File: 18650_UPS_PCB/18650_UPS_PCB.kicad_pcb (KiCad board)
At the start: 4 copper layers, 90 x 27.5 mm, 40 parts, among them J1 USB_B_Micro, J2 Conn_01x02, J3 Conn_01x02, SW1 SW_DIP_x02, U1 STLINK-V3MINI, U10 LR9102G-xx, U11 MP2667, U2 INA260, U3 EA_DOGS104N-A, U5 STM32L151RCTx

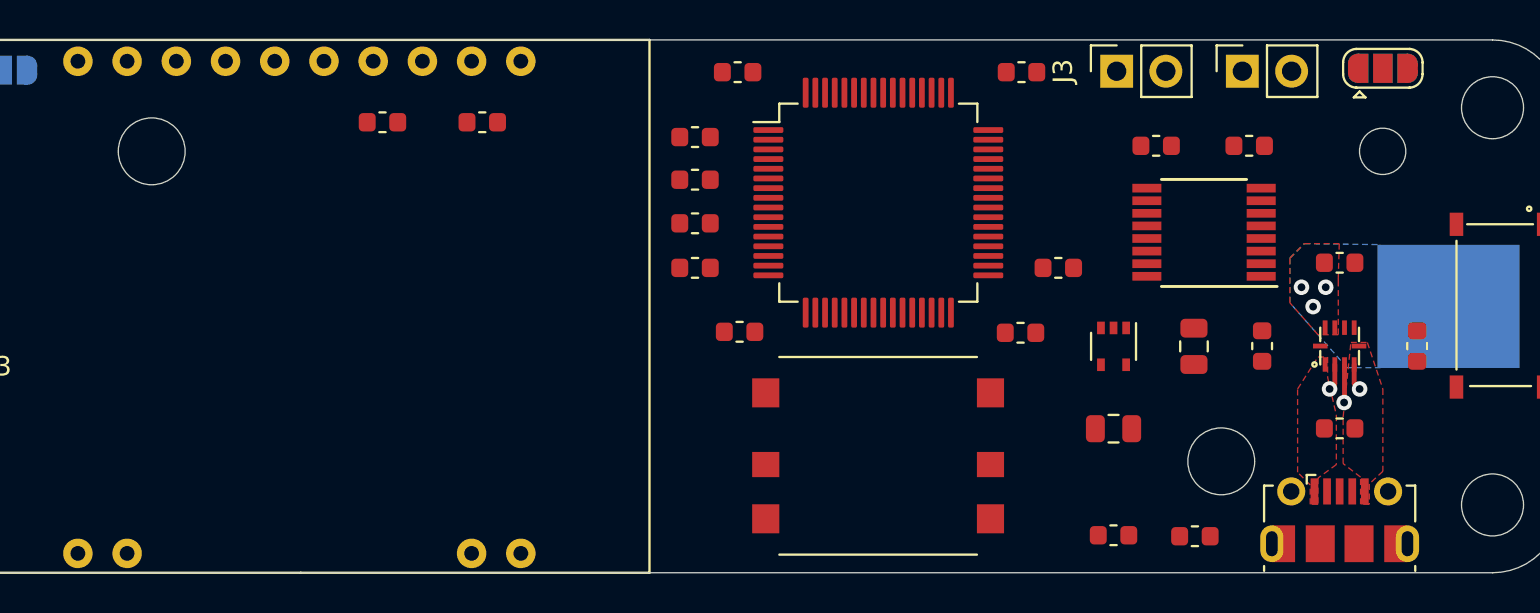
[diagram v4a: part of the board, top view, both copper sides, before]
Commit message: changed to ina 237/239
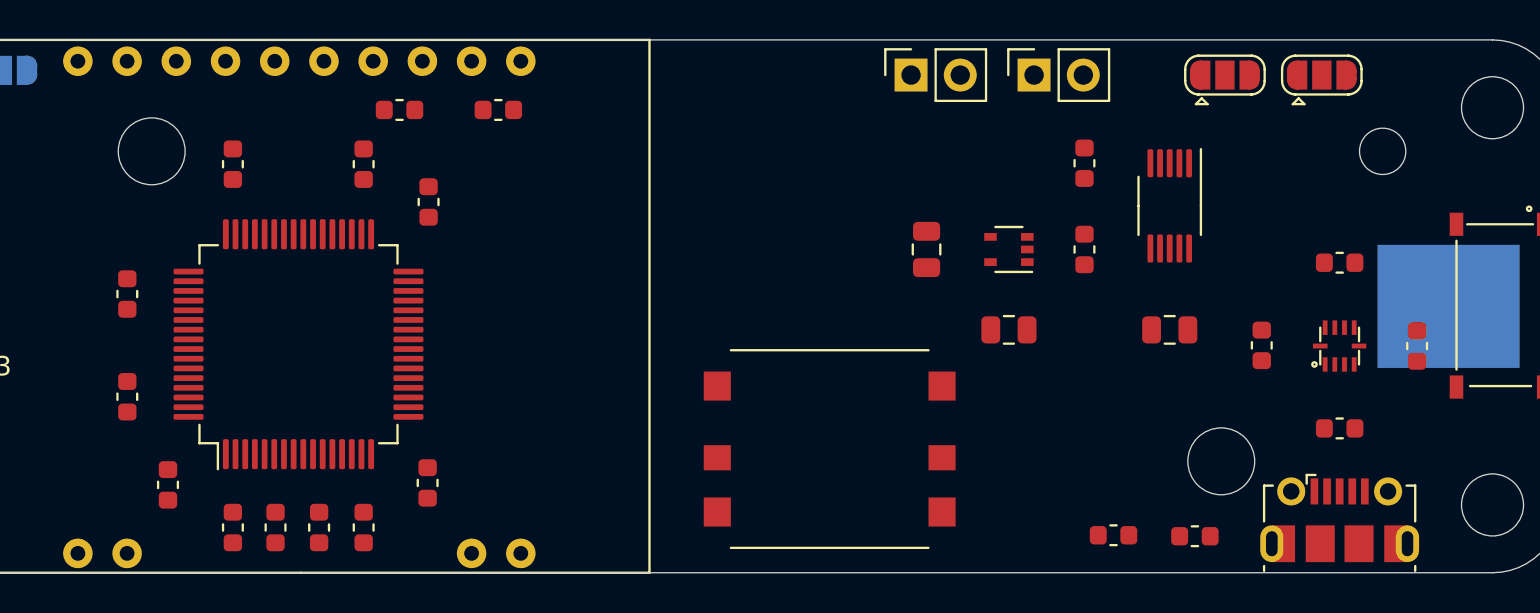
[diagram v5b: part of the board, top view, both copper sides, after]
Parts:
- added R3: 10 kOhm, Resistor_SMD:R_0603_1608Metric, F.Cu at (186.2, 80.5)
- added R4: 10 kOhm, Resistor_SMD:R_0603_1608Metric, F.Cu at (136.8, 87.3)
- added R5: 10 kOhm, Resistor_SMD:R_0603_1608Metric, F.Cu at (136.8, 92.6)
- JP2: moved to F.Cu
- R1: value 10 kOhm -> 0.01 Ohm; footprint Resistor_SMD:R_0603_1608Metric -> Resistor_SMD:R_0805_2012Metric
- U2: value INA260 -> INA237; footprint Package_SO:TSSOP-16_4.4x5mm_P0.65mm -> Package_SO:VSSOP-10_3x3mm_P0.5mm
- moved C14 41.0 mm to (142.3, 80.6), turned to 90 degrees
- moved C16 36.3 mm to (138.9, 97.2), turned to 270 degrees
- moved C7 36.2 mm to (149.1, 80.6), turned to 90 degrees
- moved C12 31.3 mm to (152.4, 82.5), turned to 90 degrees
- moved R2 31.2 mm to (142.3, 99.3), turned to 90 degrees
- moved U5 30.8 mm to (145.7, 89.9), turned to 90 degrees
- moved C5 28.1 mm to (144.5, 99.3), turned to 270 degrees
- moved C18 25.0 mm to (146.8, 99.3), turned to 270 degrees
- moved C17 21.7 mm to (149.1, 99.3), turned to 270 degrees
- moved C9 17.9 mm to (152.3, 97.0), turned to 270 degrees
- moved J2 17.1 mm to (177.3, 76.0)
- moved C8 13.4 mm to (178.1, 85.0), turned to 90 degrees
- moved R1 10.3 mm to (190.7, 89.2), turned to 180 degrees
- moved C6 9.59 mm to (182.3, 89.2), turned to 180 degrees
- moved JP1 8.16 mm to (193.5, 76.0)
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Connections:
- R1 pad 1: +3V3 -> IN+
- R1 pad 2: INA-ALERT -> IN-
- U2 pad 1: IN+ -> Net-(JP2-Pad2)
- U2 pad 10: +3V3 -> IN+
- U2 pad 2: IN+ -> Net-(JP1-Pad2)
- U2 pad 3: IN+ -> INA-ALERT
- U2 pad 4: Net-(JP2-Pad2) -> I2C1_SDA
- U2 pad 5: Net-(JP1-Pad2) -> I2C1_SCL
- U2 pad 6: GND -> +3V3
- U2 pad 7: INA-ALERT -> GND
- U2 pad 8: I2C1_SDA -> IN-
- U2 pad 9: I2C1_SCL -> IN-
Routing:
- net MP-INT: track 1.97 -> 0.00 mm, vias 1 -> 0
- net Net-(C11-Pad1): track 1.38 -> 0.00 mm, vias 1 -> 0
- net Net-(R8-Pad2): track 1.38 -> 0.00 mm, vias 1 -> 0
- net Net-(BT1-Pad1): vias 3 -> 0
- removed copper zone on F.Cu, net GND
- removed copper zone on In1.Cu, net GND
- removed copper zone on B.Cu, net Net-(BT1-Pad1)
- removed copper zone on F.Cu, net Net-(BT1-Pad1)
- removed copper zone on F.Cu, net VBUS

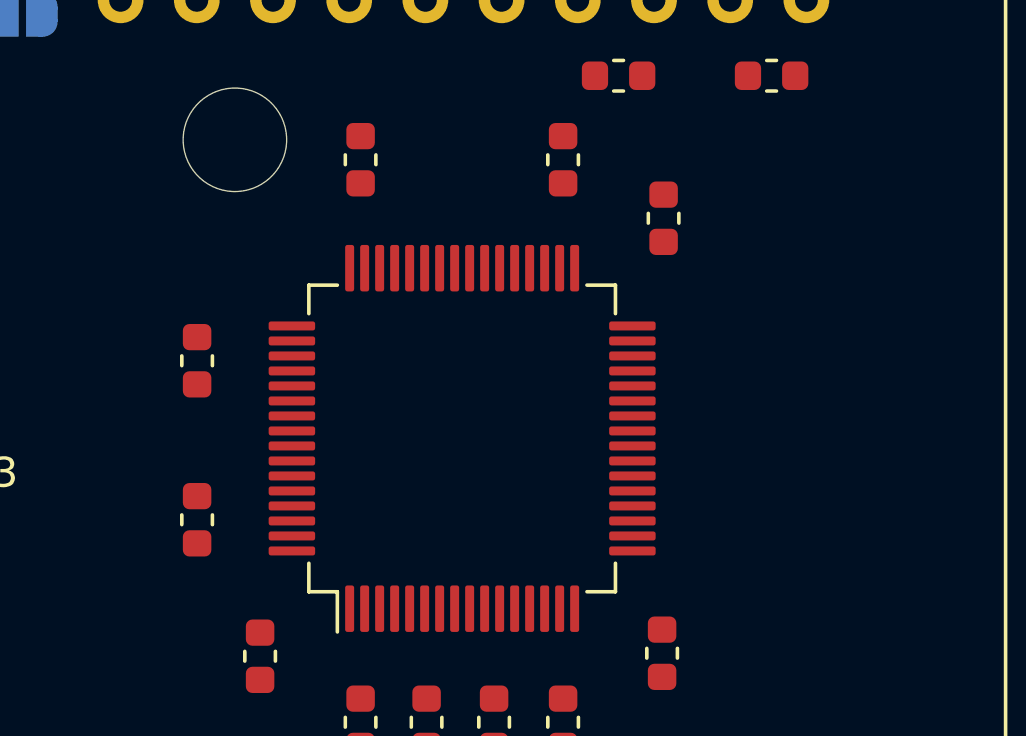
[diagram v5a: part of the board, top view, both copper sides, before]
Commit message: minor changes in layout
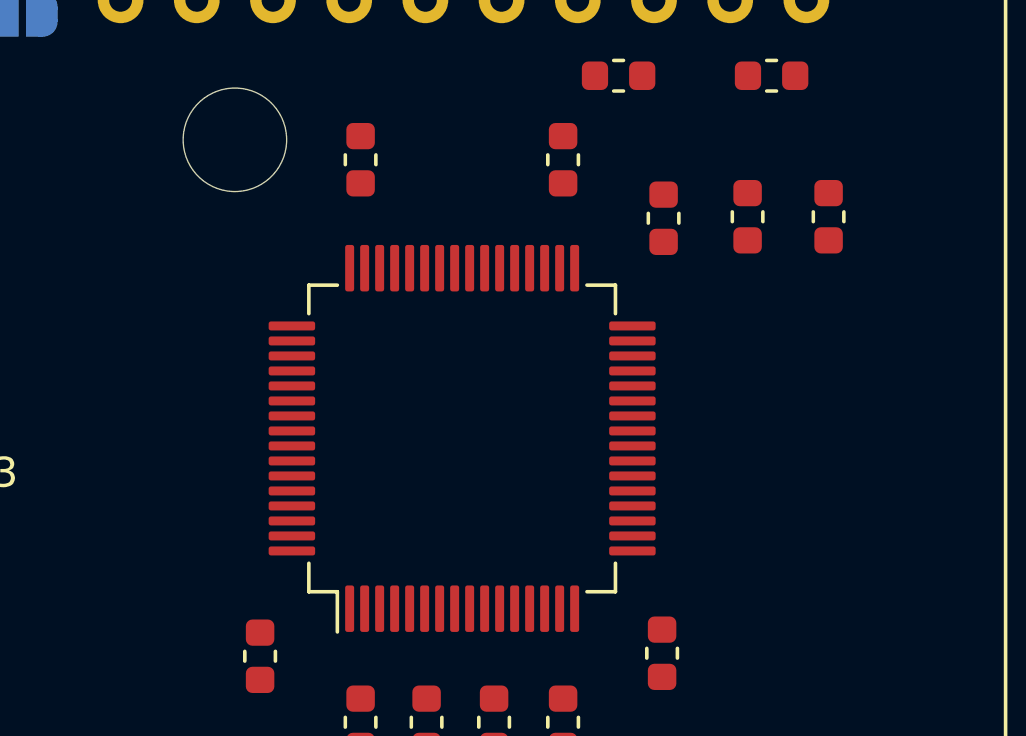
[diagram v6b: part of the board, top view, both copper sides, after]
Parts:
- moved R4 21.6 mm to (157.9, 82.5)
- moved R5 20.9 mm to (155.2, 82.5), turned to 270 degrees
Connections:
- U5 pad 17: (no net) -> TM-D
- U5 pad 20: (no net) -> TM-C
- U5 pad 21: (no net) -> TM-B
- U5 pad 22: EA-RST -> TM-A
- U5 pad 23: (no net) -> TM-Center
- U5 pad 29: (no net) -> I2C1_SCL
- U5 pad 30: TM-Center -> I2C1_SDA
- U5 pad 33: TM-A -> (no net)
- U5 pad 34: TM-B -> (no net)
- U5 pad 35: TM-C -> (no net)
- U5 pad 36: TM-D -> (no net)
- U5 pad 41: (no net) -> EA-RST
- U5 pad 42: USART1_TX -> (no net)
- U5 pad 43: USART1_RX -> (no net)
- U5 pad 58: I2C1_SCL -> USART1_TX
- U5 pad 59: I2C1_SDA -> USART1_RX

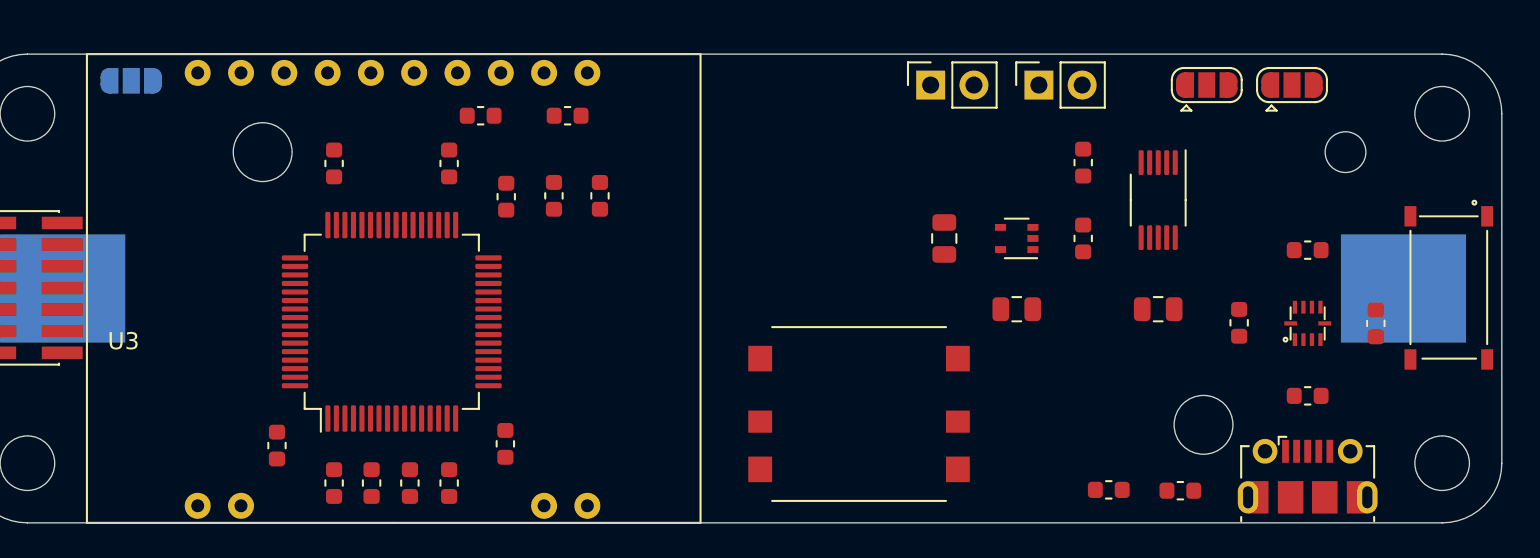
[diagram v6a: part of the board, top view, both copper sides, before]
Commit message: added silkscreen markings
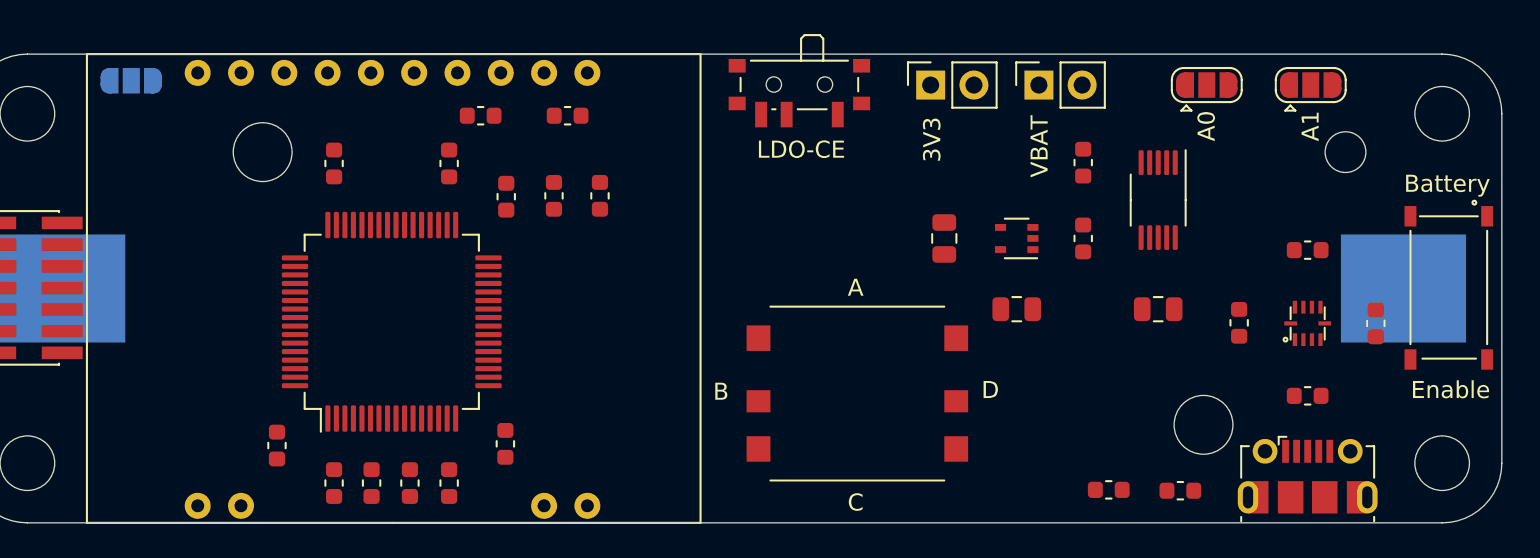
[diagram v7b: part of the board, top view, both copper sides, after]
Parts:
- added LDO1: SW_SPDT, Button_Switch_SMD:SW_SPDT_PCM12, F.Cu at (169.6, 76.3)
- moved S1 1.20 mm to (173.0, 94.1)
- moved JP2 1.10 mm to (199.6, 76.0)
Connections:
- JP1 pad 1: GND -> +3V3
- JP1 pad 3: +3V3 -> GND
- U10 pad 3: IN- -> LDO-CE
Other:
- board text added: "3V3"
- board text added: "A"
- board text added: "A0"
- board text added: "A1"
- board text added: "B"
- board text added: "Battery"
- board text added: "C"
- board text added: "D"
- board text added: "Enable"
- board text added: "LDO-CE"
- board text added: "VBAT"
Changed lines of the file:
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@@
   (general
     (thickness 1.6)
-    (drawings 8)
+    (drawings 19)
     (tracks 0)
     (zones 0)
-    (modules 43)
-    (nets 30)
+    (modules 44)
+    (nets 31)
   )
   (page A4)
@@
   (net 28 EA-RST)
   (net 29 VBUS)
+  (net 30 LDO-CE)
   (net_class Default "This is the default net class."
     (clearance 0.2)
@@
     (add_net IN-)
     (add_net INA-ALERT)
+    (add_net LDO-CE)
     (add_net MP-INT)
     (add_net NRST)
@@
     (add_net VBUS)
   )
+  (module Button_Switch_SMD:SW_SPDT_PCM12 (layer F.Cu)
+    (at 169.6 76.3 180)
+    (descr "Ultraminiature Surface Mount Slide Switch, right-angle, https://www.ckswitches.com/media/1424/pcm.pdf")
+    (attr smd)
+    (fp_text reference LDO1 (at 1.8 4.5) (layer F.SilkS) hide
+      (effects (font (size 1 1) (thickness 0.15)))
+    )
+    (fp_text value SW_SPDT (at 0 4.25) (layer F.Fab)
+      (effects (font (size 1 1) (thickness 0.15)))
+    )
+    (fp_line (start 3.45 0.72) (end 3.45 -0.07) (layer F.SilkS) (width 0.12))
+    (fp_line (start -3.45 -0.07) (end -3.45 0.72) (layer F.SilkS) (width 0.12))
+    (fp_line (start -1.6 -1.12) (end 0.1 -1.12) (layer F.SilkS) (width 0.12))
+    (fp_line (start -2.85 1.73) (end 2.85 1.73) (layer F.SilkS) (width 0.12))
+    (fp_line (start -0.1 3.02) (end -0.1 1.73) (layer F.SilkS) (width 0.12))
+    (fp_line (start -1.2 3.23) (end -0.3 3.23) (layer F.SilkS) (width 0.12))
+    (fp_line (start -1.4 1.73) (end -1.4 3.02) (layer F.SilkS) (width 0.12))
+    (fp_line (start -0.1 3.02) (end -0.3 3.23) (layer F.SilkS) (width 0.12))
+    (fp_line (start -1.4 3.02) (end -1.2 3.23) (layer F.SilkS) (width 0.12))
+    (fp_line (start -4.4 2.1) (end -4.4 -2.45) (layer F.CrtYd) (width 0.05))
+    (fp_line (start -1.65 2.1) (end -4.4 2.1) (layer F.CrtYd) (width 0.05))
+    (fp_line (start -1.65 3.4) (end -1.65 2.1) (layer F.CrtYd) (width 0.05))
+    (fp_line (start 1.65 3.4) (end -1.65 3.4) (layer F.CrtYd) (width 0.05))
+    (fp_line (start 1.65 2.1) (end 1.65 3.4) (layer F.CrtYd) (width 0.05))
+    (fp_line (start 4.4 2.1) (end 1.65 2.1) (layer F.CrtYd) (width 0.05))
+    (fp_line (start 4.4 -2.45) (end 4.4 2.1) (layer F.CrtYd) (width 0.05))
+    (fp_line (start -4.4 -2.45) (end 4.4 -2.45) (layer F.CrtYd) (width 0.05))
+    (fp_line (start 1.4 -1.12) (end 1.6 -1.12) (layer F.SilkS) (width 0.12))
+    (fp_line (start 3.35 -1) (end -3.35 -1) (layer F.Fab) (width 0.1))
+    (fp_line (start 3.35 1.6) (end 3.35 -1) (layer F.Fab) (width 0.1))
+    (fp_line (start -3.35 1.6) (end 3.35 1.6) (layer F.Fab) (width 0.1))
+    (fp_line (start -3.35 -1) (end -3.35 1.6) (layer F.Fab) (width 0.1))
+    (fp_line (start -0.1 2.9) (end -0.1 1.6) (layer F.Fab) (width 0.1))
+    (fp_line (start -0.15 2.95) (end -0.1 2.9) (layer F.Fab) (width 0.1))
+    (fp_line (start -0.35 3.15) (end -0.15 2.95) (layer F.Fab) (width 0.1))
+    (fp_line (start -1.2 3.15) (end -0.35 3.15) (layer F.Fab) (width 0.1))
+    (fp_line (start -1.4 2.95) (end -1.2 3.15) (layer F.Fab) (width 0.1))
+    (fp_line (start -1.4 1.65) (end -1.4 2.95) (layer F.Fab) (width 0.1))
+    (fp_text user %R (at 0 -3.2) (layer F.Fab)
+      (effects (font (size 1 1) (thickness 0.15)))
+    )
+    (pad "" smd rect (at -3.65 -0.78 180) (size 1 0.8) (layers F.Cu F.Paste F.Mask))
+    (pad "" smd rect (at 3.65 -0.78 180) (size 1 0.8) (layers F.Cu F.Paste F.Mask))
+    (pad "" smd rect (at 3.65 1.43 180) (size 1 0.8) (layers F.Cu F.Paste F.Mask))
+    (pad "" smd rect (at -3.65 1.43 180) (size 1 0.8) (layers F.Cu F.Paste F.Mask))
+    (pad 3 smd rect (at 2.25 -1.43 180) (size 0.7 1.5) (layers F.Cu F.Paste F.Mask)
+      (net 11 GND))
+    (pad 2 smd rect (at 0.75 -1.43 180) (size 0.7 1.5) (layers F.Cu F.Paste F.Mask)
+      (net 30 LDO-CE))
+    (pad 1 smd rect (at -2.25 -1.43 180) (size 0.7 1.5) (layers F.Cu F.Paste F.Mask)
+      (net 12 IN-))
+    (pad "" np_thru_hole circle (at 1.5 0.33 180) (size 0.9 0.9) (drill 0.9) (layers *.Cu *.Mask))
+    (pad "" np_thru_hole circle (at -1.5 0.33 180) (size 0.9 0.9) (drill 0.9) (layers *.Cu *.Mask))
+    (model ${KISYS3DMOD}/Button_Switch_SMD.3dshapes/SW_SPDT_PCM12.wrl
+      (at (xyz 0 0 0))
+      (scale (xyz 1 1 1))
+      (rotate (xyz 0 0 0))
+    )
+  )
   (module Package_SO:VSSOP-10_3x3mm_P0.5mm (layer F.Cu)
     (at 190.65 82.75 270)
@@
   (module CUSTOM_FOOTPRINTS:EA_DOGS104N-A (layer F.Cu)
     (at 134.3 100.685)
-    (fp_text reference U3 (at -4.35 -9.65) (layer F.SilkS)
+    (fp_text reference U3 (at -4.35 -9.65) (layer F.SilkS) hide
       (effects (font (size 1 1) (thickness 0.15)))
     )
@@
   )
   (module CUSTOM_FOOTPRINTS:TM-2027 (layer F.Cu)
-    (at 173.1 95.3)
+    (at 173 94.1)
     (fp_text reference S1 (at -2.6 -6.4) (layer F.SilkS) hide
       (effects (font (size 1 1) (thickness 0.15)))
@@
   )
   (module Jumper:SolderJumper-3_P1.3mm_Open_RoundedPad1.0x1.5mm (layer F.Cu)
-    (at 198.5 76)
+    (at 199.6 76)
     (descr "SMD Solder 3-pad Jumper, 1x1.5mm rounded Pads, 0.3mm gap, open")
     (tags "solder jumper open")
@@
       (net 15 "Net-(JP1-Pad2)"))
     (pad 3 smd custom (at 1.3 0) (size 1 0.5) (layers F.Cu F.Mask)
-      (net 1 +3V3) (zone_connect 2)
+      (net 11 GND) (zone_connect 2)
       (options (clearance outline) (anchor rect))
       (primitives
@@
       ))
     (pad 1 smd custom (at -1.3 0) (size 1 0.5) (layers F.Cu F.Mask)
-      (net 11 GND) (zone_connect 2)
+      (net 1 +3V3) (zone_connect 2)
       (options (clearance outline) (anchor rect))
       (primitives
@@
       (net 11 GND))
     (pad 3 smd rect (at -0.95 0.65 180) (size 0.65 0.4) (layers F.Cu F.Paste F.Mask)
-      (net 12 IN-))
+      (net 30 LDO-CE))
     (pad 1 smd rect (at -0.95 -0.65 180) (size 0.65 0.4) (layers F.Cu F.Paste F.Mask)
       (net 12 IN-))
@@
     )
   )
+  (gr_text A1 (at 199.6 78.4 90) (layer F.SilkS)
+    (effects (font (size 1 1) (thickness 0.15)))
+  )
+  (gr_text A0 (at 193.5 78.4 90) (layer F.SilkS)
+    (effects (font (size 1 1) (thickness 0.15)))
+  )
+  (gr_text C (at 172.9 100.5) (layer F.SilkS)
+    (effects (font (size 1 1) (thickness 0.15)))
+  )
+  (gr_text D (at 180.8 93.9) (layer F.SilkS)
+    (effects (font (size 1 1) (thickness 0.15)))
+  )
+  (gr_text B (at 165 94) (layer F.SilkS)
+    (effects (font (size 1 1) (thickness 0.15)))
+  )
+  (gr_text A (at 172.9 87.9) (layer F.SilkS)
+    (effects (font (size 1 1) (thickness 0.15)))
+  )
+  (gr_text Enable (at 207.8 93.9) (layer F.SilkS)
+    (effects (font (size 1 1) (thickness 0.15)))
+  )
+  (gr_text Battery (at 207.6 81.8) (layer F.SilkS)
+    (effects (font (size 1 1) (thickness 0.15)))
+  )
+  (gr_text LDO-CE (at 169.7 79.8) (layer F.SilkS)
+    (effects (font (size 1 1) (thickness 0.15)))
+  )
+  (gr_text VBAT (at 183.7 79.6 90) (layer F.SilkS)
+    (effects (font (size 1 1) (thickness 0.15)))
+  )
+  (gr_text 3V3 (at 177.4 79.2 90) (layer F.SilkS)
+    (effects (font (size 1 1) (thickness 0.15)))
+  )
   (gr_line (start 207.31 101.685) (end 124.31 101.685) (layer Edge.Cuts) (width 0.05))
